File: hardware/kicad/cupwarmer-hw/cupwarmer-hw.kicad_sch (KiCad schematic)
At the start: 0 parts

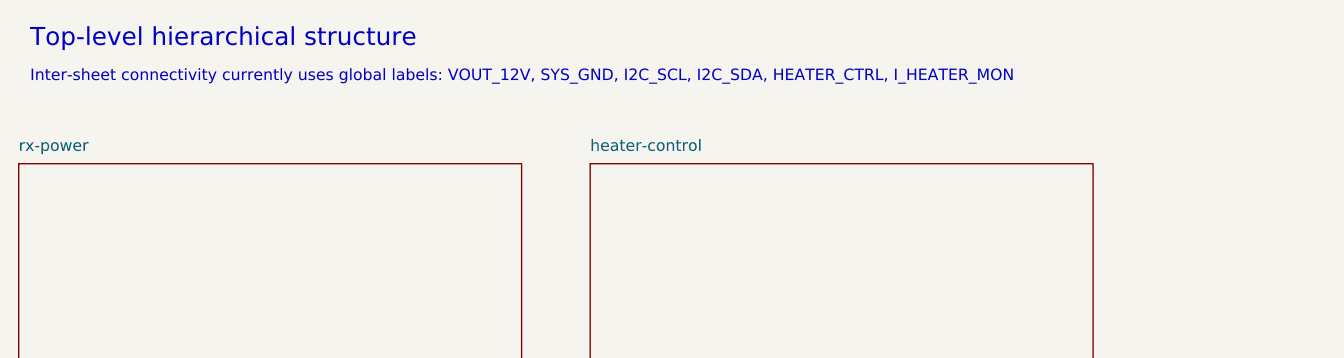
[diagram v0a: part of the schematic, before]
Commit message: Update design notes and sheet annotations for v1 decisions
- design-notes: record cup contact layer choice (alumina-filled silicone
  pad) and close out LED-2/INTB indicator decision (D2 driven from
  RX_VAA -> R11 -> GPIO0; INTB exposed via J3 only, no LED driver)
- cupwarmer-hw root sheet: refresh key global labels annotation
- sensors-logic: reword "first spin" -> "v1" for consistency
- rx-power: nudge R10 down 1.27mm to clear surrounding labels

Co-Authored-By: Claude Opus 4.7 (1M context) <noreply@anthropic.com>
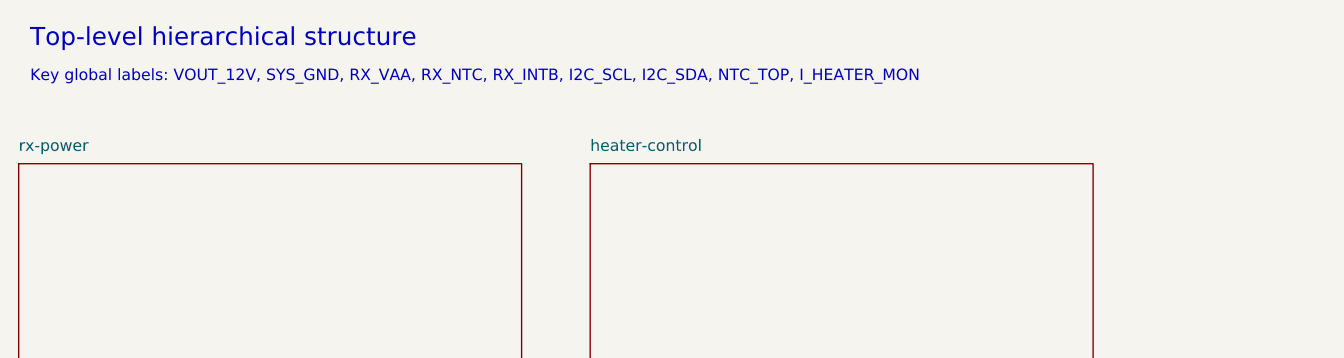
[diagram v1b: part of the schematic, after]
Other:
- note added: "Key global labels: VOUT_12V, SYS_GND, RX_VAA, RX_NTC, RX_INTB, I2C_SCL, I2C_SDA, NTC_TOP, I_HEATER_MON"
- note removed: "Inter-sheet connectivity currently uses global labels: VOUT_12V, SYS_GND, I2C_SCL, I2C_SDA, HEATER_CTRL, I_HEATER_MON"
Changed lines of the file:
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@@
 		)
 	)
-	(text "Inter-sheet connectivity currently uses global labels: VOUT_12V, SYS_GND, I2C_SCL, I2C_SDA, HEATER_CTRL, I_HEATER_MON"
+	(text "Key global labels: VOUT_12V, SYS_GND, RX_VAA, RX_NTC, RX_INTB, I2C_SCL, I2C_SDA, NTC_TOP, I_HEATER_MON"
 		(exclude_from_sim no)
 		(at 39.37 35.56 0)

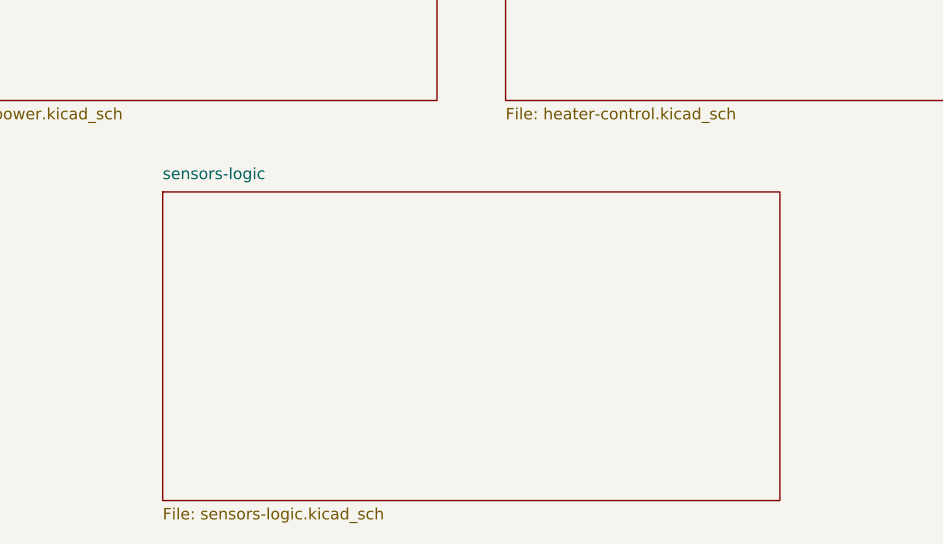
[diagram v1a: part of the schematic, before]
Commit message: Merge sensors-logic into rx-power; delete sensors-logic sheet
sensors-logic had only 3 symbols left after the THERM_MON cleanup
(J1 I2C service header, J3 status header, TH2 100k NTC).
Move them into rx-power and remove the sub-sheet.

- rx-power.kicad_sch: add J1 (152.4, 170.18), J3 (152.4, 185.42),
  TH2 (76.2, 175.26) with their global labels (RX_VAA, SYS_GND,
  I2C_SCL, I2C_SDA, RX_INTB, RX_NTC, I_HEATER_MON) preserved
- cupwarmer-hw.kicad_sch: remove sensors-logic sheet block
- delete sensors-logic.kicad_sch and sensors-logic.kicad_prl

ERC: 0 errors, 0 warnings. Netlist node membership unchanged
(verified via kicad-tool sch validate baseline diff).

PCB intentionally not updated; sync via KiCad GUI.

Co-Authored-By: Claude Opus 4.7 (1M context) <noreply@anthropic.com>
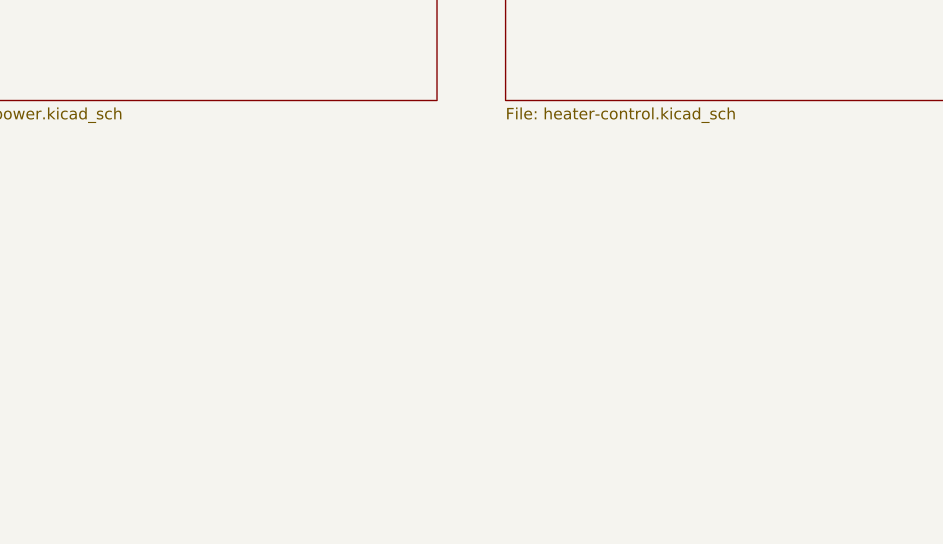
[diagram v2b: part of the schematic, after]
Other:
- removed sheet sensors-logic
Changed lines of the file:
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@@
-		)
-	)
-	(sheet
-		(at 63.5 88.9)
-		(size 68.58 34.29)
-		(exclude_from_sim no)
-		(in_bom yes)
-		(on_board yes)
-		(dnp no)
-		(stroke
-			(width 0.1524)
-			(type solid)
-		)
-		(fill
-			(color 0 0 0 0)
-		)
-		(property "Sheetname" "sensors-logic"
-			(at 63.5 87.63 0)
-			(show_name no)
-			(do_not_autoplace no)
-			(effects
-				(font
-					(size 1.27 1.27)
-					(thickness 0.15)
-				)
-				(justify left bottom)
-			)
-		)
-		(property "Sheetfile" "sensors-logic.kicad_sch"
-			(at 63.5 123.952 0)
-			(show_name no)
-			(do_not_autoplace no)
-			(effects
-				(font
-					(size 1.27 1.27)
-					(thickness 0.15)
-				)
-				(justify left top)
-			)
 		)
 	)
